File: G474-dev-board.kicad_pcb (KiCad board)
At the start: 4 copper layers, 70 x 82.5 mm, 79 parts, among them J1 Conn_01x03, J10 USB_C_Receptacle_USB2.0_16P, J11 Conn_01x02, J12 EXT_PWR, J13 Conn_02x03_Odd_Even, J14 Conn_01x02, J15 Conn_01x02, J16 Conn_01x02, J2 Conn_01x02, J3 Conn_01x08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

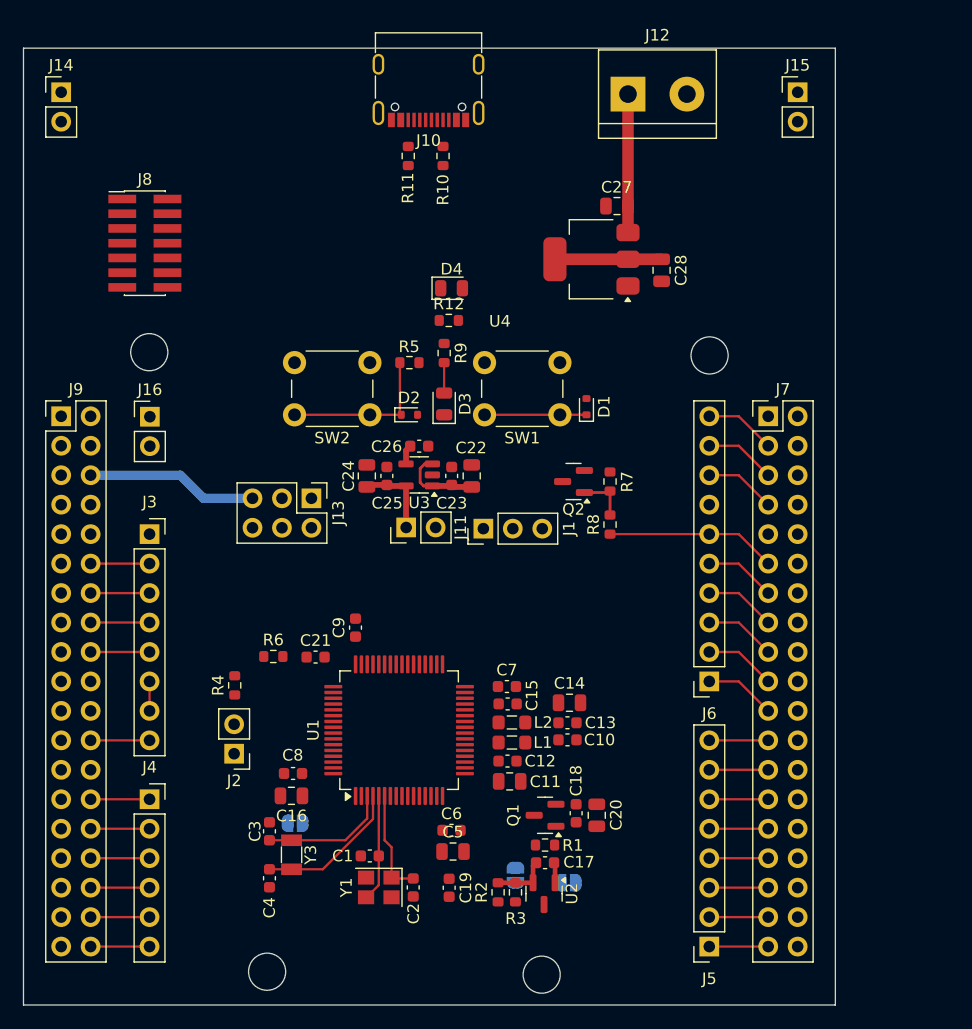
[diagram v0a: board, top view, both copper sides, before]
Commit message: SMD part number assigned, relocate MCU sch to hierarcical sheet
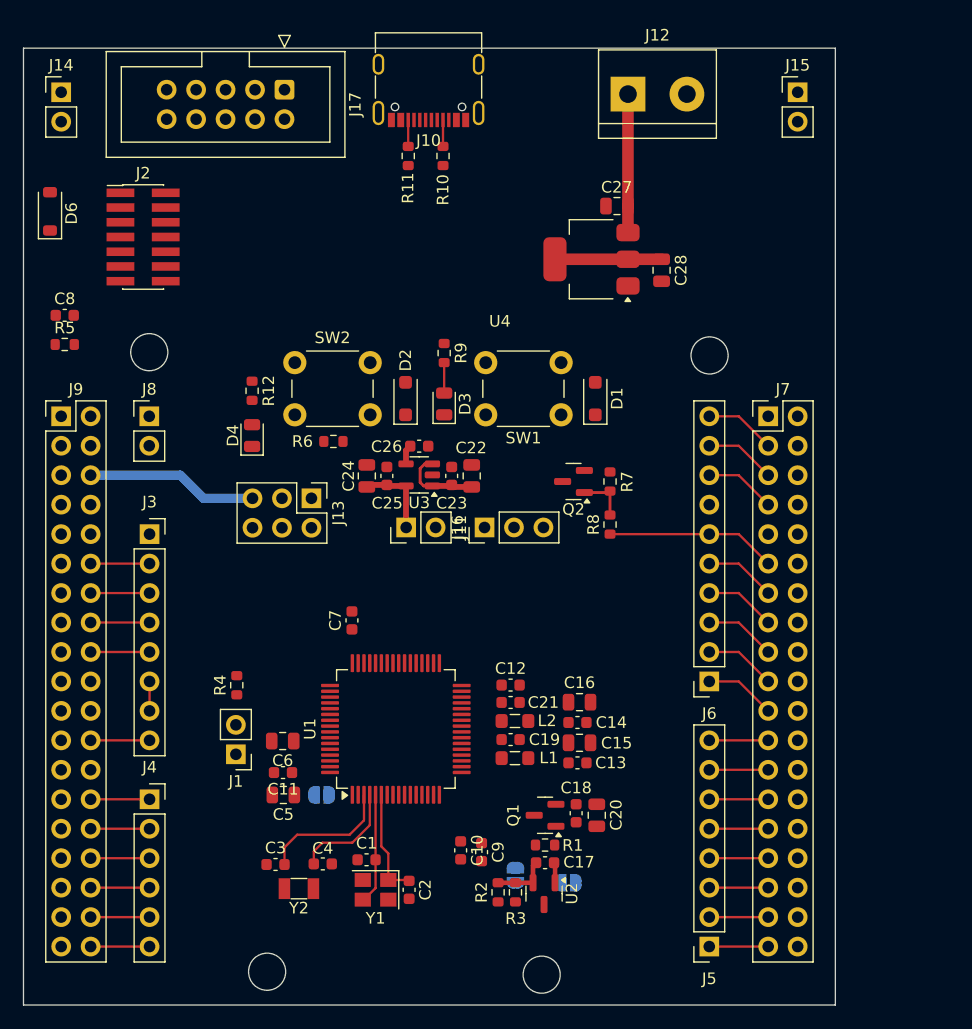
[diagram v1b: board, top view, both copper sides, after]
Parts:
- removed Y3: 32.768KHz, Crystal:Crystal_SMD_3215-2Pin_3.2x1.5mm
- added D6: MBR0520, Diode_SMD:D_SOD-123, F.Cu at (104.4, 72.7)
- added J17: Conn_02x05_Odd_Even, Connector_IDC:IDC-Header_2x05_P2.54mm_Vertical, F.Cu at (124.7, 62.2)
- added Y2: 32.768KHz, Crystal:Crystal_SMD_3215-2Pin_3.2x1.5mm, F.Cu at (125.9, 131.1)
- C11, C14: value 1u -> 100n; footprint Capacitor_SMD:C_0805_2012Metric -> Capacitor_SMD:C_0603_1608Metric
- C15: value 100n -> 1u; footprint Capacitor_SMD:C_0603_1608Metric -> Capacitor_SMD:C_0805_2012Metric
- C5: value 4.7u -> 1u
- C6: value 100n -> 4.7u; footprint Capacitor_SMD:C_0603_1608Metric -> Capacitor_SMD:C_0805_2012Metric
- D1, D2: footprint Diode_SMD:D_SOD-523 -> Diode_SMD:D_SOD-123F
- D3: value LED -> RED
- D4: value LED -> GREEN
- J1: value Conn_01x03 -> Conn_01x02; footprint Connector_PinHeader_2.54mm:PinHeader_1x03_P2.54mm_Vertical -> Connector_PinHeader_2.54mm:PinHeader_1x02_P2.54mm_Vertical
- J16: value Conn_01x02 -> Conn_01x03; footprint Connector_PinHeader_2.54mm:PinHeader_1x02_P2.54mm_Vertical -> Connector_PinHeader_2.54mm:PinHeader_1x03_P2.54mm_Vertical
- J2: value Conn_01x02 -> ST-LINK; footprint Connector_PinHeader_2.54mm:PinHeader_1x02_P2.54mm_Vertical -> Connector_PinHeader_1.27mm:PinHeader_2x07_P1.27mm_Vertical_SMD
- J8: value ST-LINK -> Conn_01x02; footprint Connector_PinHeader_1.27mm:PinHeader_2x07_P1.27mm_Vertical_SMD -> Connector_PinHeader_2.54mm:PinHeader_1x02_P2.54mm_Vertical
- R5: value 100K -> 330
- R6: value 330 -> 100K
- moved J2 45.2 mm to (112.5, 74.9), turned to 0 degrees
- moved C8 44.1 mm to (105.7, 81.7), turned to 0 degrees
- moved J16 30.4 mm to (141.9, 100.0), turned to 90 degrees
- moved R5 29.8 mm to (105.7, 84.2)
- moved J1 28.9 mm to (120.5, 119.5), turned to 180 degrees
- moved C16 26.1 mm to (150.1, 115.0), turned to 0 degrees
- moved C9 22.2 mm to (141.7, 128.0), turned to -90 degrees
- moved D4 21.4 mm to (121.9, 92.0), turned to 90 degrees
- moved C11 19.6 mm to (124.5, 121.1), turned to 180 degrees
- moved R6 19.3 mm to (128.9, 92.6), turned to 180 degrees
- moved R12 18.0 mm to (121.9, 88.2), turned to -90 degrees
- moved C21 17.3 mm to (144.2, 115.1)
- moved C6 16.5 mm to (124.5, 118.4), turned to 180 degrees
- moved C5 15.4 mm to (124.6, 123.0), turned to 180 degrees
- moved J8 14.9 mm to (113.0, 90.4)
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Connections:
- net /OSC32_IN renamed /MCU/OSC32_IN
- net /OSC32_OUT renamed /MCU/OSC32_OUT
- net /OSC_IN renamed /MCU/OSC_IN
- net /OSC_OUT renamed /MCU/OSC_OUT
- net /PA0 renamed /MCU/PA0
- net /PA1 renamed /MCU/PA1
- net /PA10 renamed /MCU/PA10
- net /PA11 renamed /MCU/PA11
- net /PA12 renamed /MCU/PA12
- net /PA13 renamed /MCU/PA13
- net /PA14 renamed /MCU/PA14
- net /PA15 renamed /MCU/PA15
- net /PA2 renamed /MCU/PA2
- net /PA3 renamed /MCU/PA3
- net /PA4 renamed /MCU/PA4
- net /PA5 renamed /MCU/PA5
- net /PA6 renamed /MCU/PA6
- net /PA7 renamed /MCU/PA7
- net /PA8 renamed /MCU/PA8
- net /PA9 renamed /MCU/PA9
- net /PB0 renamed /MCU/PB0
- net /PB1 renamed /MCU/PB1
- net /PB10 renamed /MCU/PB10
- net /PB11 renamed /MCU/PB11
- net /PB12 renamed /MCU/PB12
- net /PB13 renamed /MCU/PB13
- net /PB14 renamed /MCU/PB14
- net /PB15 renamed /MCU/PB15
- net /PB2 renamed /MCU/PB2
- net /PB3 renamed /MCU/PB3
- net /PB4 renamed /MCU/PB4
- net /PB5 renamed /MCU/PB5
- net /PB6 renamed /MCU/PB6
- net /PB7 renamed /MCU/PB7
- net /PB9 renamed /MCU/PB9
- net /PC0 renamed /MCU/PC0
- net /PC1 renamed /MCU/PC1
- net /PC10 renamed /MCU/PC10
- net /PC11 renamed /MCU/PC11
- net /PC12 renamed /MCU/PC12
- net /PC13 renamed /MCU/PC13
- net /PC2 renamed /MCU/PC2
- net /PC3 renamed /MCU/PC3
- net /PC4 renamed /MCU/PC4
- net /PC5 renamed /MCU/PC5
- net /PC6 renamed /MCU/PC6
- net /PC7 renamed /MCU/PC7
- net /PC8 renamed /MCU/PC8
- net /PC9 renamed /MCU/PC9
- net /PD2 renamed /MCU/PD2
- C10 pad 1: Net-(J1-Pin_2) -> /MCU/NRST
- C11 pad 1: +VDDREF -> +3V3
- C12 pad 1: +VDDREF -> +3V3
- C13 pad 1: +3V3 -> Net-(J16-Pin_2)
- C14 pad 1: +VDDA -> +3V3
- C15 pad 1: +VDDA -> +VDDREF
- C16 pad 1: /VBAT -> +VDDA
- C19 pad 1: /NRST -> +VDDREF
- C21 pad 1: /BTN_USER -> +VDDA
- C5 pad 1: +3V3 -> /MCU/VBAT
- C8 pad 1: +3V3 -> /MCU/BTN_USER
- D1 pad 1: /NRST -> /MCU/NRST
- J1 pad 1: +VREF -> /MCU/PB8
- J1 pad 2: Net-(J1-Pin_2) -> /MCU/BOOT
- J16 pad 1: unconnected-(J16-Pin_1-Pad1) -> +VREF
- J16 pad 2: unconnected-(J16-Pin_2-Pad2) -> Net-(J16-Pin_2)
- J2 pad 1: /PB8 -> Net-(D6-A)
- J2 pad 2: /BOOT -> GND
- JP1 pad 1: /VBAT -> /MCU/VBAT
- L1 pad 1: Net-(J1-Pin_2) -> Net-(J16-Pin_2)
- R4 pad 1: /BOOT -> /MCU/BOOT
- R5 pad 1: Net-(D2-K) -> /MCU/BTN_USER
- R5 pad 2: GND -> Net-(D2-K)
- R6 pad 1: /BTN_USER -> Net-(D2-K)
- R6 pad 2: Net-(D2-K) -> GND
- SW1 pad 1: /NRST -> /MCU/NRST
- U1 pad 1: /VBAT -> /MCU/VBAT
- U1 pad 61: /PB8 -> /MCU/PB8
- U1 pad 7: /NRST -> /MCU/NRST
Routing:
- net Net-(D2-K): track 13.8 -> 0.00 mm
- net /NRST: track 8.79 -> 0.00 mm
- net /MCU/OSC32_OUT: track 12.7 -> 9.46 mm
- net Net-(J10-CC2): track 0.00 -> 2.28 mm
- net Net-(J10-CC1): track 0.00 -> 2.28 mm

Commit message: no changes
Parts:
- moved C24 9.28 mm to (141.0, 94.8)
- moved C22 9.11 mm to (131.7, 94.8), turned to -90 degrees
- moved C23 5.67 mm to (133.5, 94.8), turned to -90 degrees
- moved C25 5.59 mm to (139.0, 94.8), turned to -90 degrees
- moved J16 5.09 mm to (147.0, 100.0), turned to -90 degrees
- moved C26 4.45 mm to (136.3, 97.4), turned to 180 degrees
- moved C9 3.53 mm to (138.8, 125.9), turned to 180 degrees
- moved R12 3.25 mm to (121.9, 84.9)
- moved D4 2.73 mm to (121.9, 89.3)
- moved J11 2.67 mm to (137.8, 100.0), turned to -90 degrees
- moved C10 2.50 mm to (137.9, 129.4)
- moved C13 1.96 mm to (149.9, 118.3), turned to 180 degrees
- moved C15 1.94 mm to (149.9, 120.5)
- moved J6 1.03 mm to (161.3, 114.3)
- moved C11 1.00 mm to (125.5, 120.8), turned to 90 degrees
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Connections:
- net /MCU/PA2 renamed /IO/PA2
- net /MCU/PA3 renamed /IO/PA3
- net /MCU/PB8 renamed /IO/PB8
- net /MCU/PC10 renamed /IO/PC10
- C10 pad 1: /MCU/NRST -> /IO/NRST
- D1 pad 1: /MCU/NRST -> /IO/NRST
- J1 pad 2: /MCU/BOOT -> /IO/BOOT
- J2 pad 12: /MCU/NRST -> /IO/NRST
- J9 pad 33: /IO/VBAT -> /MCU/VBAT
- R4 pad 1: /MCU/BOOT -> /IO/BOOT
- SW1 pad 1: /MCU/NRST -> /IO/NRST
- U1 pad 10: /MCU/PC2 -> /IO/PC2
- U1 pad 11: /MCU/PC3 -> /IO/PC3
- U1 pad 12: /MCU/PA0 -> /IO/PA0
- U1 pad 13: /MCU/PA1 -> /IO/PA1
- U1 pad 18: /MCU/PA4 -> /IO/PA4
- U1 pad 19: /MCU/PA5 -> /IO/PA5
- U1 pad 2: /MCU/PC13 -> /IO/PC13
- U1 pad 20: /MCU/PA6 -> /IO/PA6
- U1 pad 21: /MCU/PA7 -> /IO/PA7
- U1 pad 22: /MCU/PC4 -> /IO/PC4
- U1 pad 23: /MCU/PC5 -> /IO/PC5
- U1 pad 24: /MCU/PB0 -> /IO/PB0
- U1 pad 25: /MCU/PB1 -> /IO/PB1
- U1 pad 26: /MCU/PB2 -> /IO/PB2
- U1 pad 30: /MCU/PB10 -> /IO/PB10
- U1 pad 33: /MCU/PB11 -> /IO/PB11
- U1 pad 34: /MCU/PB12 -> /IO/PB12
- U1 pad 35: /MCU/PB13 -> /IO/PB13
- U1 pad 36: /MCU/PB14 -> /IO/PB14
- U1 pad 37: /MCU/PB15 -> /IO/PB15
- U1 pad 38: /MCU/PC6 -> /IO/PC6
- U1 pad 39: /MCU/PC7 -> /IO/PC7
- U1 pad 40: /MCU/PC8 -> /IO/PC8
- U1 pad 41: /MCU/PC9 -> /IO/PC9
- U1 pad 42: /MCU/PA8 -> /IO/PA8
- U1 pad 43: /MCU/PA9 -> /IO/PA9
- U1 pad 44: /MCU/PA10 -> /IO/PA10
- U1 pad 45: /MCU/PA11 -> /IO/PA11
- U1 pad 46: /MCU/PA12 -> /IO/PA12
- U1 pad 49: /MCU/PA13 -> /IO/PA13
- U1 pad 50: /MCU/PA14 -> /IO/PA14
- U1 pad 51: /MCU/PA15 -> /IO/PA15
- U1 pad 53: /MCU/PC11 -> /IO/PC11
- U1 pad 54: /MCU/PC12 -> /IO/PC12
- U1 pad 55: /MCU/PD2 -> /IO/PD2
- U1 pad 56: /MCU/PB3 -> /IO/PB3
- U1 pad 57: /MCU/PB4 -> /IO/PB4
- U1 pad 58: /MCU/PB5 -> /IO/PB5
- U1 pad 59: /MCU/PB6 -> /IO/PB6
- U1 pad 60: /MCU/PB7 -> /IO/PB7
- U1 pad 62: /MCU/PB9 -> /IO/PB9
- U1 pad 7: /MCU/NRST -> /IO/NRST
- U1 pad 8: /MCU/PC0 -> /IO/PC0
- U1 pad 9: /MCU/PC1 -> /IO/PC1
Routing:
- net GND: track 2.54 -> 55.1 mm, vias 0 -> 42
- net +VREF: track 0.00 -> 31.9 mm
- net Net-(J16-Pin_2): track 0.00 -> 29.5 mm
- net Net-(D3-K): track 0.00 -> 24.8 mm
- net +3V3: track 0.00 -> 22.2 mm, vias 0 -> 6
- net /IO/NRST: track 5.08 -> 24.6 mm, vias 0 -> 1
- net +5V: track 7.10 -> 23.9 mm
- net Net-(D2-K): track 0.00 -> 13.9 mm
- net +VDDREF: track 6.13 -> 19.1 mm
- net +VDDA: track 0.00 -> 11.7 mm
- net /MCU/VBAT: track 0.00 -> 5.78 mm
- net Net-(Q1-B): track 1.76 -> 4.87 mm
- net Net-(J11-Pin_1): track 7.07 -> 9.89 mm
- net Net-(D4-A): track 0.00 -> 2.62 mm
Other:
- board text added: "3V3"
- board text added: "5V"
- board text added: "A0"
- board text added: "A1"
- board text added: "A2"
- board text added: "A3"
- board text added: "A4"
- board text added: "A5"
- board text added: "AIN"
- board text added: "D2"
- board text added: "D4"
- board text added: "D7"
- board text added: "D8"
- board text added: "GND"
- board text added: "MISO/D12"
- board text added: "NRST"
- board text added: "POWER"
- board text added: "PWM/CS/D10"
- board text added: "PWM/D3"
- board text added: "PWM/D5"
- board text added: "PWM/D6"
- board text added: "PWM/D9"
- board text added: "PWM/MOSI/D11"
- board text added: "RX/D0"
- board text added: "SCK/D13"
- board text added: "SCL/D15"
- board text added: "SDA/D14"
- board text added: "TX/D1"
- board text added: "VIN"
- board text added: "VREF"

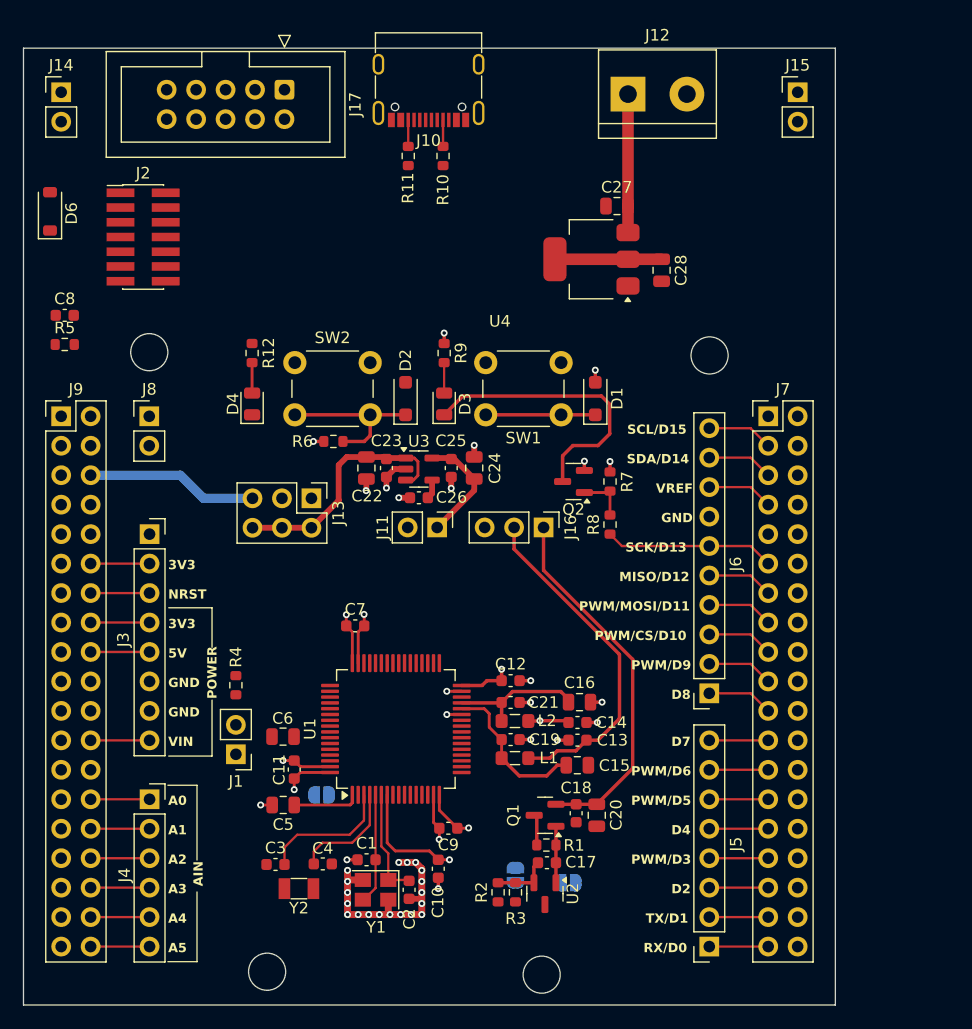
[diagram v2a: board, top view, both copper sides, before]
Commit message: IO tracks routed, 2 pin left
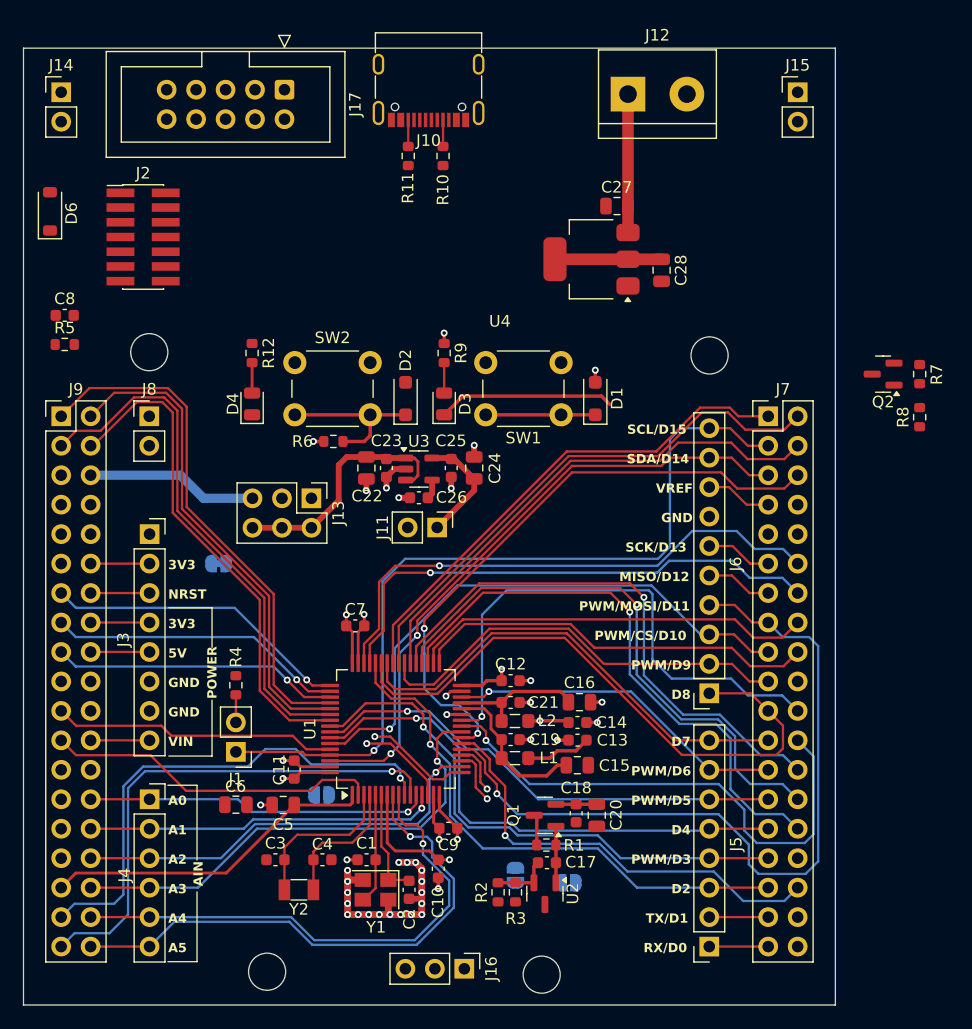
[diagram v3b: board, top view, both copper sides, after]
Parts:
- added JP4: JMP_SHRT, Jumper:SolderJumper-2_P1.3mm_Bridged_RoundedPad1.0x1.5mm, B.Cu at (119.0, 103.1)
- moved J16 38.7 mm to (140.2, 138.0)
- moved Q2 28.3 mm to (176.3, 86.8)
- moved R7 28.3 mm to (179.4, 86.8)
- moved R8 28.3 mm to (179.4, 90.5)
- moved C6 7.14 mm to (120.5, 123.9)
- moved C3 0.41 mm to (123.9, 128.6)
- moved C4 0.36 mm to (127.9, 128.6)
- moved J1 0.21 mm to (120.5, 119.3)
- moved Y2 0.10 mm to (125.9, 131.2)
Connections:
- net Net-(J3-Pin_2) renamed IOREF
- J3 pad 4: Net-(J3-Pin_4) -> +3V3
- J3 pad 5: Net-(J3-Pin_5) -> +5V
- J3 pad 8: Net-(J3-Pin_8) -> +VIN
- J6 pad 10: Net-(J6-Pin_10) -> /IO/PB8
- J7 pad 3: Net-(J6-Pin_10) -> /IO/PB8
- J9 pad 1: /IO/PC0 -> /IO/PC10
- J9 pad 16: Net-(J3-Pin_4) -> +3V3
- J9 pad 18: Net-(J3-Pin_5) -> +5V
- J9 pad 24: Net-(J3-Pin_8) -> +VIN
- J9 pad 25: /IO/PC14 -> unconnected-(J9-Pin_25-Pad25)
- J9 pad 27: /IO/PC15 -> unconnected-(J9-Pin_27-Pad27)
- J9 pad 29: /IO/PF0 -> unconnected-(J9-Pin_29-Pad29)
- J9 pad 31: /IO/PF1 -> unconnected-(J9-Pin_31-Pad31)
- J9 pad 5: unconnected-(J9-Pin_5-Pad5) -> +3V3
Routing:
- net /IO/PB8: track 0.00 -> 71.9 mm, vias 0 -> 1
- net /IO/PA7: track 5.71 -> 67.1 mm, vias 0 -> 1
- net /IO/PC5: track 0.00 -> 52.7 mm, vias 0 -> 2
- net /IO/PB13: track 0.00 -> 49.3 mm, vias 0 -> 1
- net /IO/PB9: track 5.71 -> 54.6 mm, vias 0 -> 2
- net /IO/PB14: track 0.00 -> 48.6 mm, vias 0 -> 1
- net /IO/PB15: track 0.00 -> 47.2 mm, vias 0 -> 1
- net /IO/PA9: track 5.71 -> 52.6 mm
- net /IO/PA12: track 0.00 -> 46.6 mm, vias 0 -> 1
- net /IO/PB2: track 0.00 -> 46.3 mm, vias 0 -> 1
- net /IO/PC8: track 0.00 -> 46.3 mm
- net /IO/PC12: track 0.00 -> 45.9 mm
- net /IO/PC10: track 0.00 -> 45.1 mm
- net /IO/PA11: track 0.00 -> 45.0 mm, vias 0 -> 1
- net /IO/PB1: track 0.00 -> 45.0 mm, vias 0 -> 1
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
